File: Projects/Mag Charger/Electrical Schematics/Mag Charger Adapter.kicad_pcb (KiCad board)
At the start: 2 copper layers, 26 x 25.7 mm, 12 parts, among them J1 Conn_01x08, P1 USB_C_Plug_USB2.0

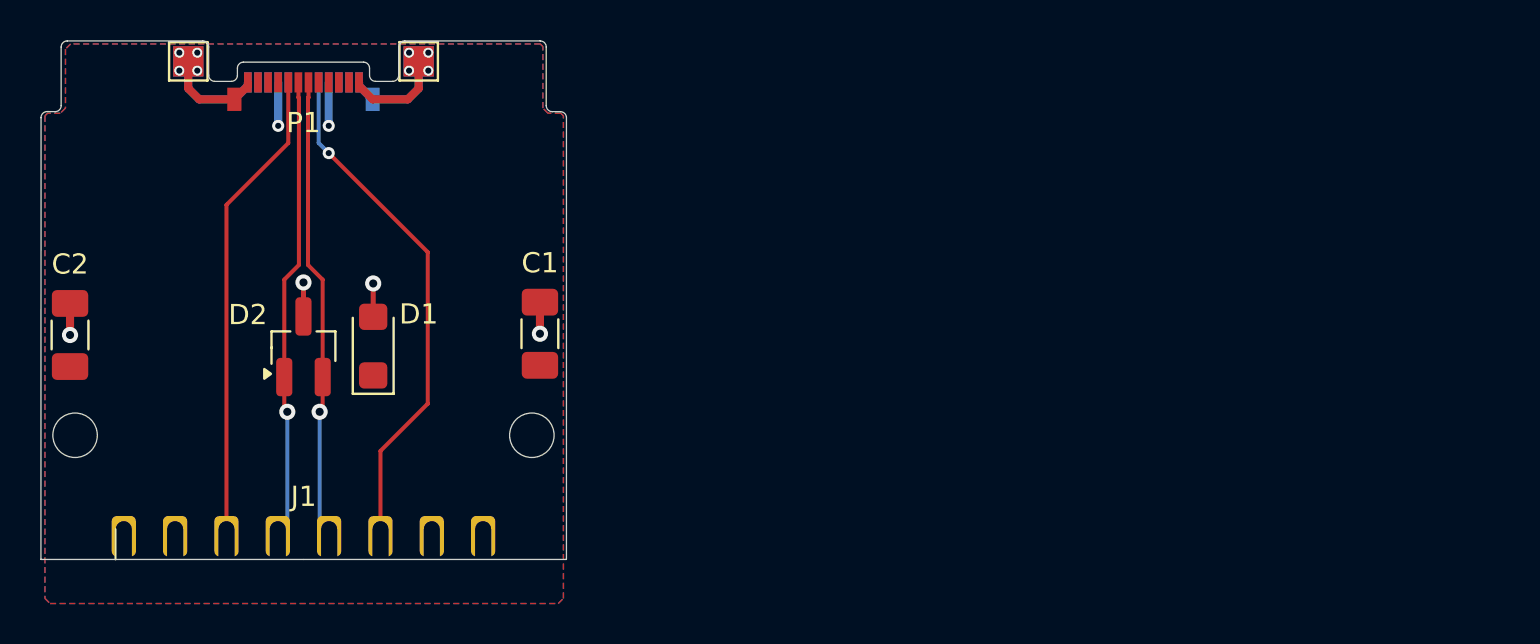
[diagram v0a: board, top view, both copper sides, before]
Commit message: Designed USB to Magnet Adapter
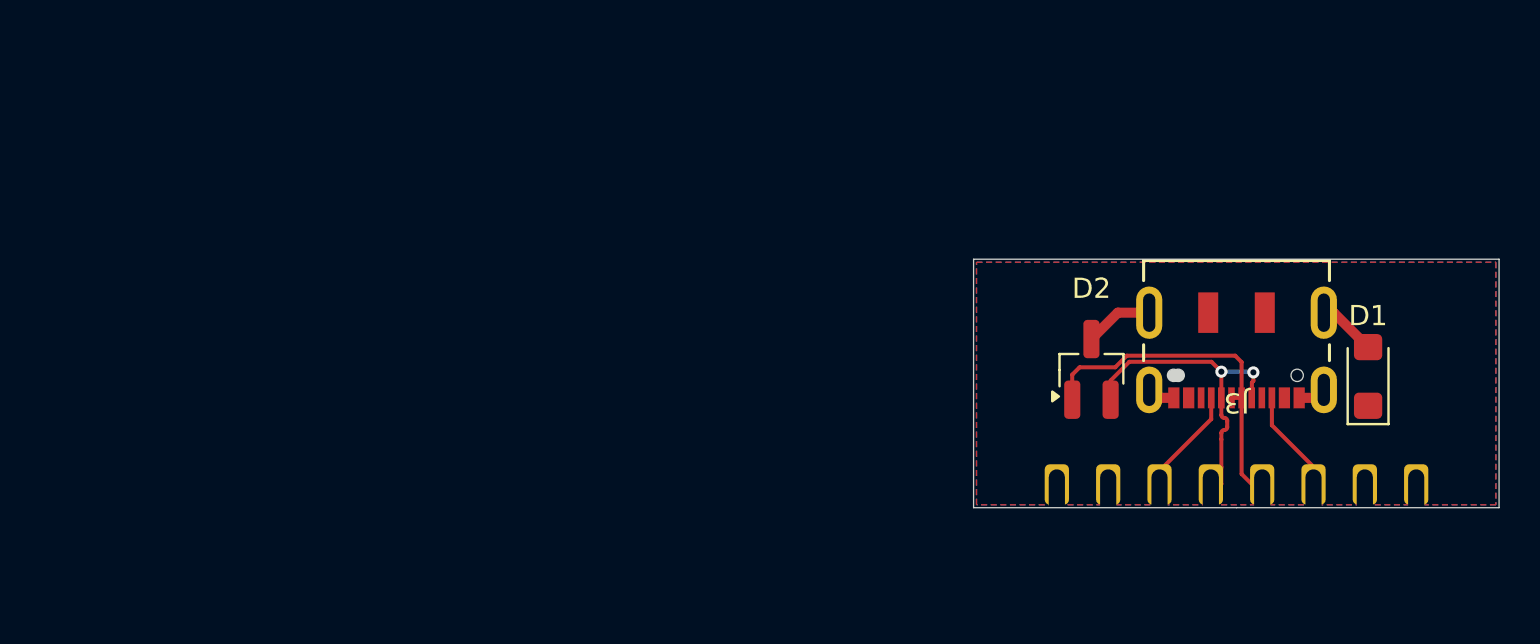
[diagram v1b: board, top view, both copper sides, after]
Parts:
- removed C1, C2: C, Capacitor_SMD:C_1206_3216Metric_Pad1.33x1.80mm_HandSolder
- removed H1, H2: MountingHole, MountingHole:MountingHole_2.2mm_M2
- removed P1: USB_C_Plug_USB2.0, Expansion_Card:USB_C_Plug_Molex_105444
- removed TP1, TP2, TP3, TP4: TestPoint, TestPoint:TestPoint_Pad_1.5x1.5mm
- added J3: DX07S016JA3R1500, Mag Charger:USB C Socket, F.Cu at (154.5, 137.4)
- J1: moved to B.Cu
- moved D1 49.2 mm to (161.0, 139.6)
- moved J1 46.2 mm to (154.5, 145.4), turned to 180 degrees
- moved D2 39.0 mm to (147.3, 139.2)
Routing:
- net /USB_VCONN: track 26.2 -> 5.84 mm, vias 1 -> 0
- net /USB_CC: track 24.2 -> 5.64 mm
- net GND: track 26.3 -> 9.06 mm, vias 12 -> 0
- net /USB_DN: track 24.0 -> 16.5 mm, vias 1 -> 2
- net /USB_DP: track 24.0 -> 17.6 mm, vias 1 -> 0
- net VBUS: track 4.86 -> 0.00 mm, vias 2 -> 0
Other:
- board size 26 x 25.7 mm -> 26 x 12.3 mm
